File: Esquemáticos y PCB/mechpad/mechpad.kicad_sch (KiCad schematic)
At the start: 0 parts

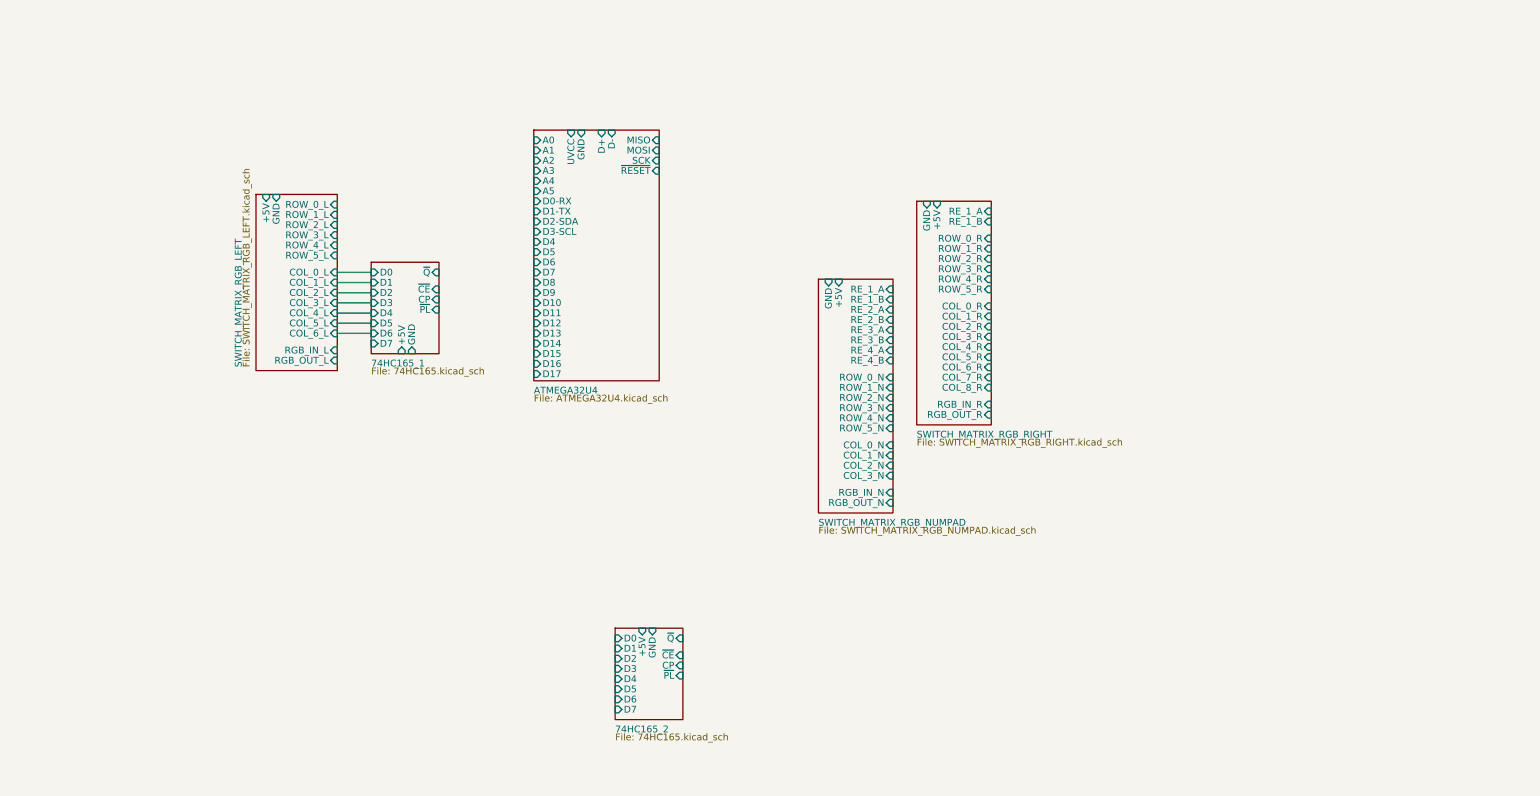
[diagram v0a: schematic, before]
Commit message: Updated schematic
Added connections between hierarchical sheets, more code testing
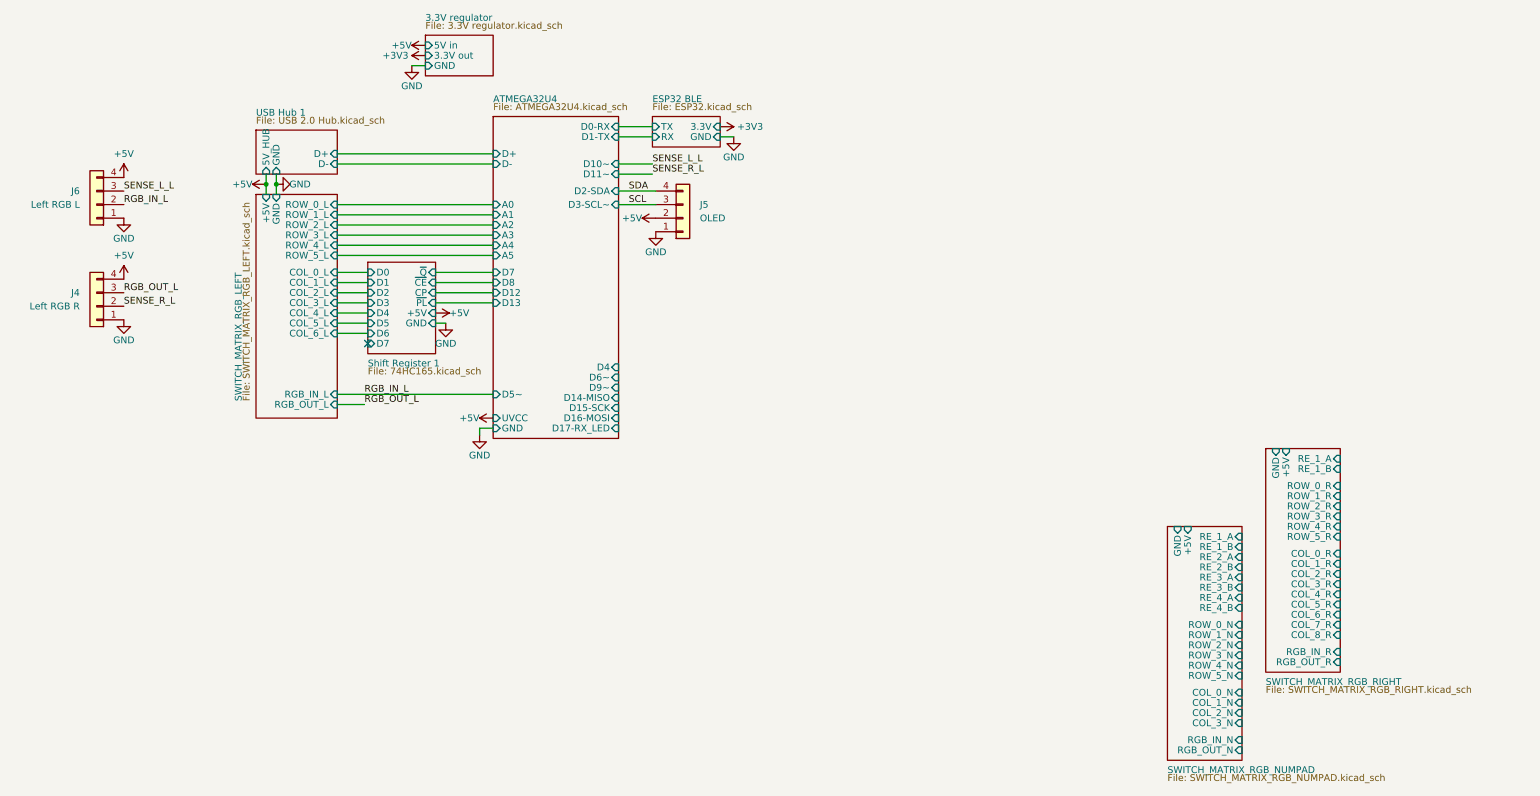
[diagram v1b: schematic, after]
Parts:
- added J4: Left RGB R, symbol Connector_Generic:Conn_01x04
- added J5: OLED, symbol Connector_Generic:Conn_01x04
- added J6: Left RGB L, symbol Connector_Generic:Conn_01x04
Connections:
- new net +5V: J4.4 (Pin_4), J5.2 (Pin_2), J6.4 (Pin_4)
- new net GND: J4.1 (Pin_1), J5.1 (Pin_1), J6.1 (Pin_1)
- new net RGB_IN_L: J6.2 (Pin_2)
- new net RGB_OUT_L: J4.3 (Pin_3)
- new net SCL: J5.3 (Pin_3)
- new net SDA: J5.4 (Pin_4)
- new net SENSE_L_L: J6.3 (Pin_3)
- new net SENSE_R_L: J4.2 (Pin_2)
- no-connect marks 0 -> 1
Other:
- sheet 74HC165_1 renamed Shift Register 1
- removed sheet 74HC165_2
- added sheet 3.3V regulator (3.3V regulator.kicad_sch)
- added sheet ESP32 BLE (ESP32.kicad_sch)
- added sheet USB Hub 1 (USB 2.0 Hub.kicad_sch)
- sheet ATMEGA32U4 ports: added D10~, D11~, D14-MISO, D15-SCK, D16-MOSI, D17-RX_LED, D3-SCL~, D5~, D6~, D9~; removed D10, D11, D14, D15, D16, D17, D3-SCL, D5, D6, D9, MISO, MOSI, SCK, ~{RESET}
